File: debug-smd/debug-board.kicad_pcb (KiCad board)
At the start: 2 copper layers, 26.7 x 27.9 mm, 10 parts, among them P1 CONN_01X04, P2 CONN_01X01

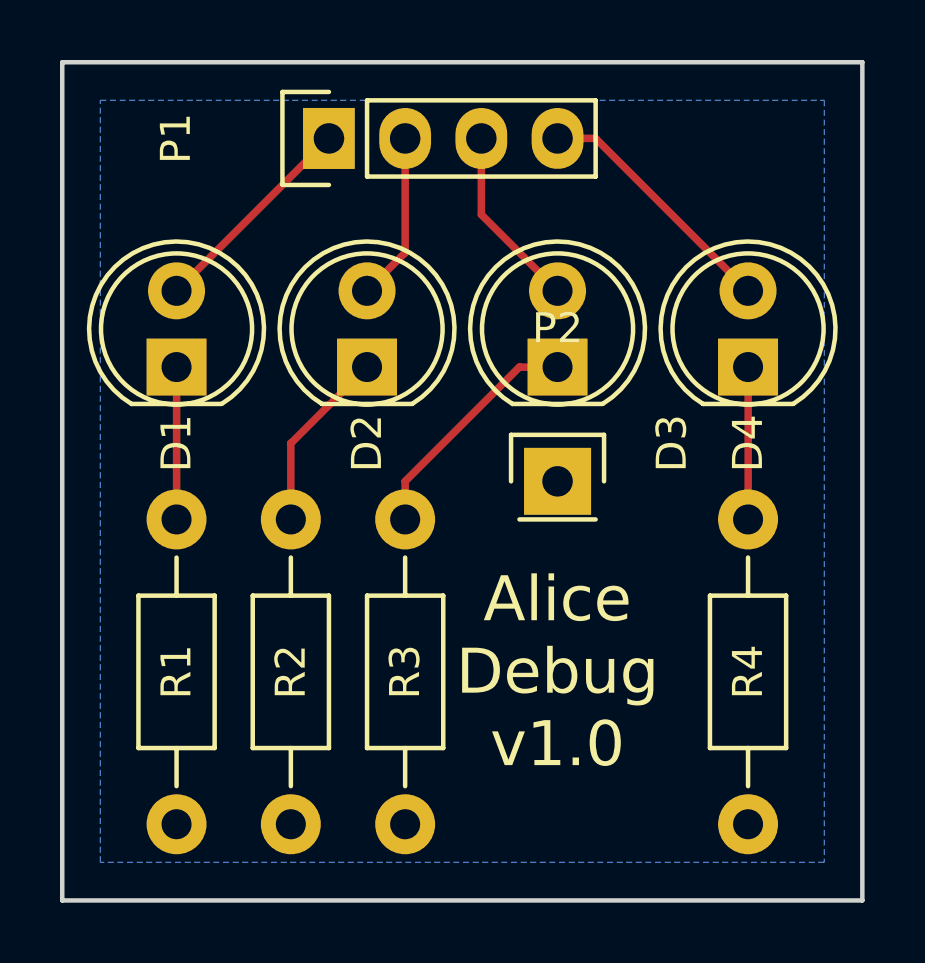
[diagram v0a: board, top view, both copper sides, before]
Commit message: Convert to SMD.
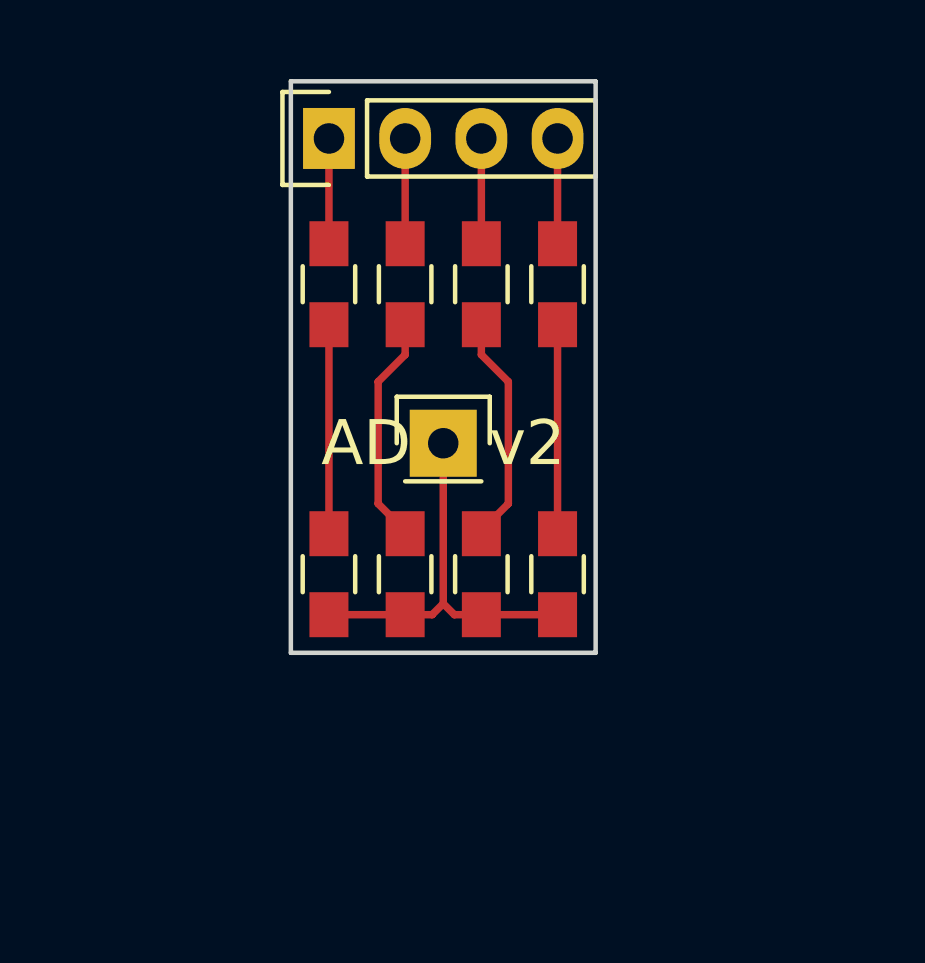
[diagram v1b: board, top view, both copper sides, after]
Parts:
- D1, D2, D3, D4: footprint LEDs:LED-5MM -> Resistors_SMD:R_0805_HandSoldering
- R1, R2, R3, R4: footprint Resistors_ThroughHole:Resistor_Horizontal_RM10mm -> Resistors_SMD:R_0805_HandSoldering
- moved R4 7.14 mm to (151.1, 104.7)
- moved D4 6.92 mm to (151.1, 95.0)
- moved R1 6.03 mm to (143.5, 104.7)
- moved D1 5.78 mm to (143.5, 95.0)
- moved R2 5.01 mm to (146.1, 104.7)
- moved R3 4.13 mm to (148.6, 104.7)
- moved P2 4.02 mm to (147.3, 100.3)
- moved D3 3.75 mm to (148.6, 95.0)
- moved D2 3.04 mm to (146.1, 95.0)
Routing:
- net GND: track 0.00 -> 13.3 mm
- net Net-(D4-Pad2): track 8.45 -> 3.81 mm
- net Net-(D1-Pad2): track 7.18 -> 3.81 mm
- net Net-(D3-Pad2): track 6.13 -> 3.81 mm
- net Net-(D2-Pad1): track 6.13 -> 8.15 mm
- net Net-(D4-Pad1): track 5.08 -> 6.97 mm
- net Net-(D1-Pad1): track 5.08 -> 6.97 mm
- net Net-(D2-Pad2): track 5.61 -> 3.81 mm
- removed copper zone on B.Cu, net GND
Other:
- board size 26.7 x 27.9 mm -> 10.2 x 19 mm
- board text added: "AD v2"
- board text removed: "Alice Debug v1.0"
